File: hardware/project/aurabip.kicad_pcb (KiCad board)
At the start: 4 copper layers, 52 x 52 mm, 50 parts, among them J1 USB-C, J2 AKKU, J3 SPEAKER, J4 OLED SPI, J5 u.FL 868, SW1 EIN/AUS, SW2 RESET, SW3 BOOT, U1 ESP32-S3-MINI-1, U10 E22-900M22S, U2 BMP581, U3 LSM6DSO32, U4 SHT40, U5 L96, U6 MAX98357A, U7 MCP73831, U8 AP2112K-3.3, U9 USBLC6

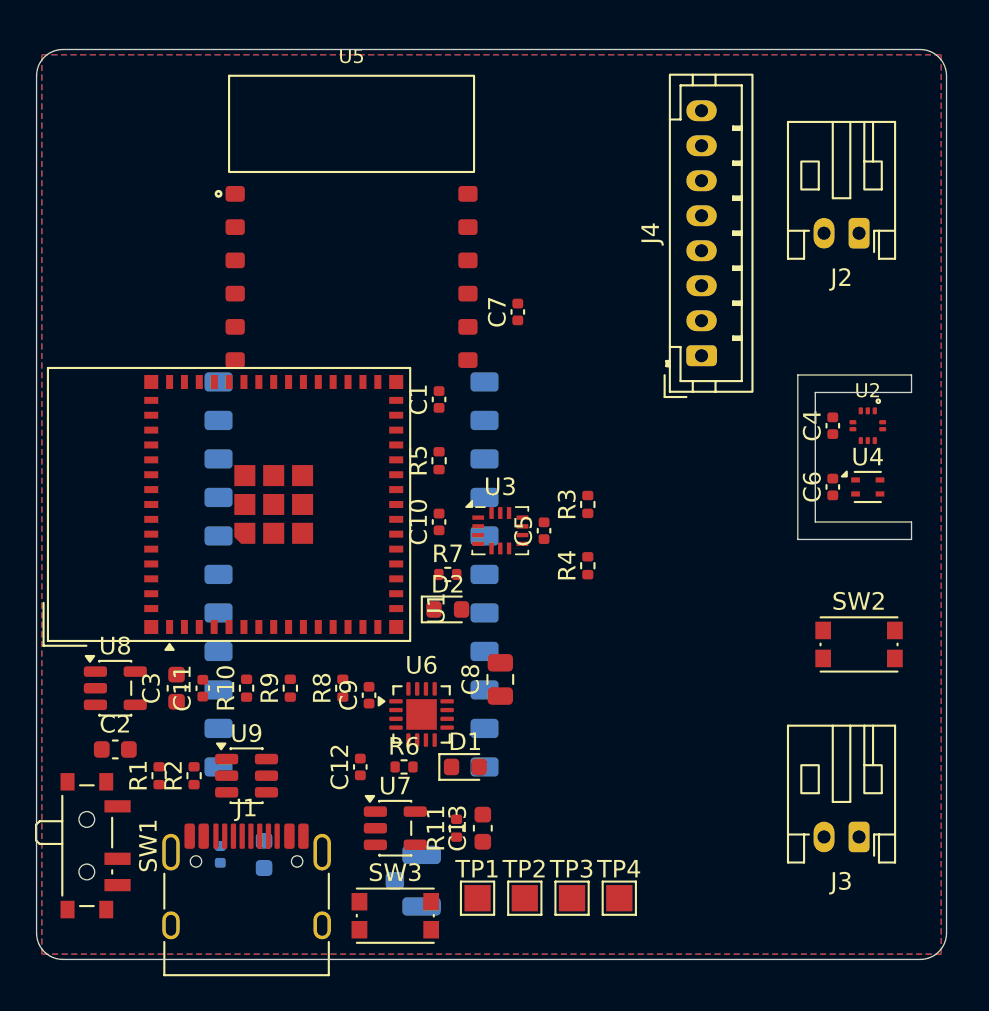
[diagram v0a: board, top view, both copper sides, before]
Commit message: fix(hardware): alle kritischen Pinouts gegen Datenblaetter verifiziert
Web-Recherche gegen Originalquellen (Ebyte Manual v1.3, Quectel HW
Design V1.4, ADI Rev 7, ST Rev 1) — drei von vier Annahmen waren falsch:
- E22-900M22S: 14x20/Pitch 1.27 statt 16x26/2.2, Pin-Map komplett neu
- L96: LCC-31 statt 12 Pads; RF-Bruecke R12 (RF_OUT->RF_IN, sonst kein
  GPS!), RXD-Pegelteiler R13/R14 (VIHmax 3.1V), C16, Antennen-Keepout
- MAX98357A: TQFN-Pinout neu (Pin 8 war VDD, nicht GND!), EP1.23-Footprint
- LSM6DSO32: Pinout bestaetigt, ST-Footprint statt Bosch (0.1mm-Versatz)

Dazu: Gehaeuse-Generator fuer Fusion 360 (hardware/fusion/, Varianten
audio/vision, Akku 504050, K-28-WP-Sitz, Antennen-Nische, Display-
Fenster), Board-STEP-Export, PCBWay-Fertigungspaket (export_fab.ps1 +
BOM-Generator), Akku auf 504050 1500mAh.

Co-Authored-By: Claude Fable 5 <noreply@anthropic.com>
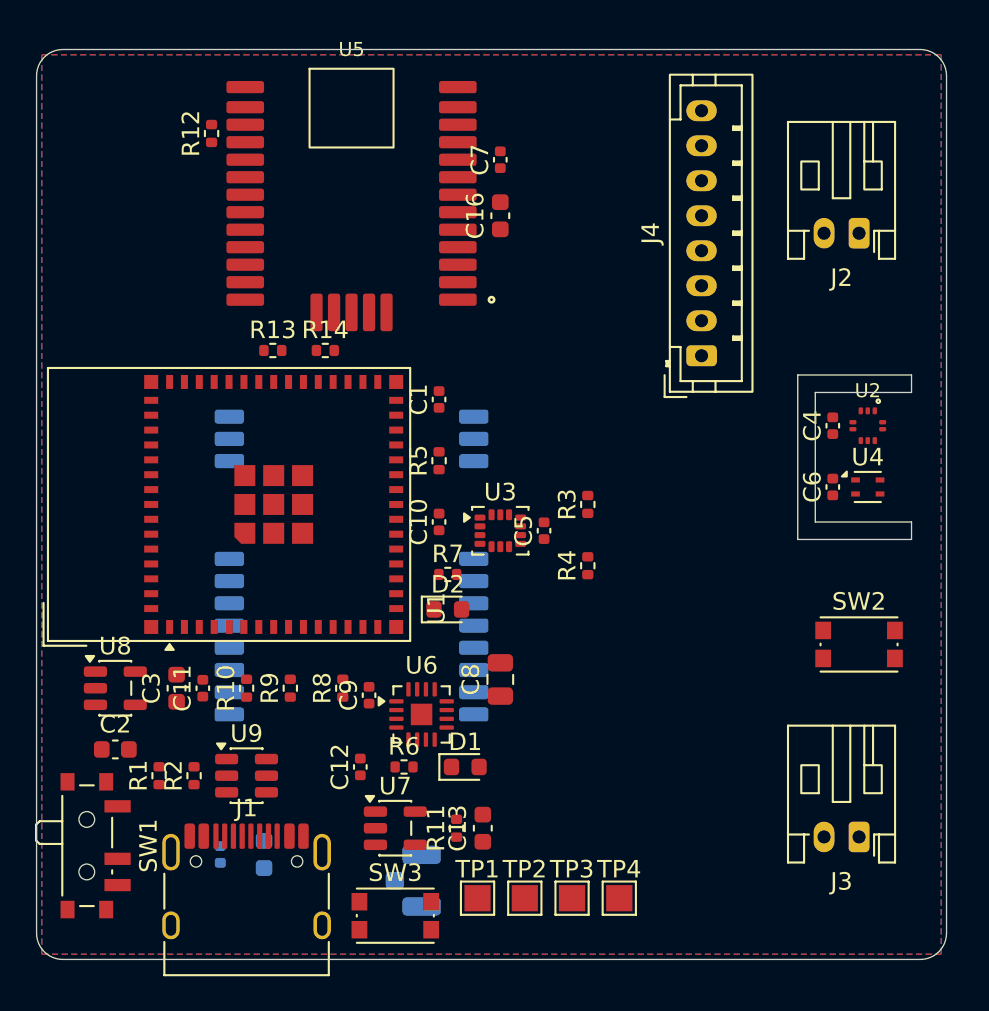
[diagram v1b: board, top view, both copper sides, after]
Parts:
- added C16: 10u, C_0603_1608Metric, F.Cu at (26.5, 9.50)
- added R12: 0R, R_0402_1005Metric, F.Cu at (10.0, 4.80)
- added R13: 1k, R_0402_1005Metric, F.Cu at (13.5, 17.2)
- added R14: 2k, R_0402_1005Metric, F.Cu at (16.5, 17.2)
- U3: footprint Bosch_LGA-14_3x2.5mm_P0.5mm -> LGA-14_3x2.5mm_P0.5mm_LayoutBorder3x4y
- U6: footprint QFN-16-1EP_3x3mm_P0.5mm_EP1.75x1.75mm -> TQFN-16-1EP_3x3mm_P0.5mm_EP1.23x1.23mm
- moved C7 8.76 mm to (26.5, 6.30)
- moved U5 0.90 mm to (18.0, 8.10)
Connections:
- U10 pad 10: LORA_RST -> GND
- U10 pad 11: +3V3 -> GND
- U10 pad 13: (no net) -> LORA_DIO1
- U10 pad 14: LORA_DIO1 -> LORA_BUSY
- U10 pad 15: LORA_BUSY -> LORA_RST
- U10 pad 21: (no net) -> LORA_ANT
- U10 pad 22: (no net) -> GND
- U10 pad 3: LORA_ANT -> GND
- U10 pad 4: (no net) -> GND
- U10 pad 5: (no net) -> GND
- U10 pad 6: LORA_TXEN -> LORA_RXEN
- U10 pad 7: LORA_RXEN -> LORA_TXEN
- U10 pad 9: (no net) -> +3V3
- U5 pad 1: GND -> (no net)
- U5 pad 10: GNSS_RXD -> GND
- U5 pad 11: (no net) -> GND
- U5 pad 3: GND -> (no net)
- U5 pad 4: (no net) -> GND
- U5 pad 5: (no net) -> GND
- U5 pad 6: +3V3 -> (no net)
- U5 pad 7: GND -> (no net)
- U5 pad 9: GNSS_TXD -> +3V3
- U6 pad 1: I2S_LRCK -> I2S_DOUT
- U6 pad 10: (no net) -> SPK_N
- U6 pad 11: SPK_N -> GND
- U6 pad 13: VBAT -> (no net)
- U6 pad 14: (no net) -> I2S_LRCK
- U6 pad 15: (no net) -> GND
- U6 pad 16: (no net) -> I2S_BCLK
- U6 pad 2: I2S_BCLK -> (no net)
- U6 pad 3: I2S_DOUT -> GND
- U6 pad 4: (no net) -> AMP_SD
- U6 pad 5: AMP_SD -> (no net)
- U6 pad 7: (no net) -> VBAT
- U6 pad 8: GND -> VBAT

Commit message: feat(route): deterministischer Rest-Router v4 + Gehaeuse v2 (Akustik)
- handroute4: exakte Rechteck-Kollisionspruefung (Pad-AABBs),
  Segment-Schnitttest (Kreuzungs-Bug behoben), Via-Routing F->B,
  Diagonal-/Dogleg-Kandidaten, Multi-Via-Spots, GND-Offset-Hookup;
  laeuft als LETZTER Pipeline-Schritt (kein FreeRouting-Roundtrip
  mehr danach — der SES-Import verwirft sonst Handrouten)
- LoRa-Bus (ESP<->E22 ueber Rueckseite) wird deterministisch gelegt
- Fusion-Gehaeuse v2: root.name-Fix, geschlossene Lautsprecher-
  Rueckkammer + Trichterfront + optionaler Reflex-Kanal (PORT),
  Antennen-Nische vertikal / optional SMA-Stummel (ANT_STUB),
  Akku 504050, J3 90 Grad gedreht (Ivo)

Co-Authored-By: Claude Fable 5 <noreply@anthropic.com>
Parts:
- moved J3 1.80 mm to (46.0, 43.5), turned to 90 degrees
